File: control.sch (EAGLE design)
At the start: 68 parts, among them IC3 ATTINY85-20S, U1 L293DD013TR

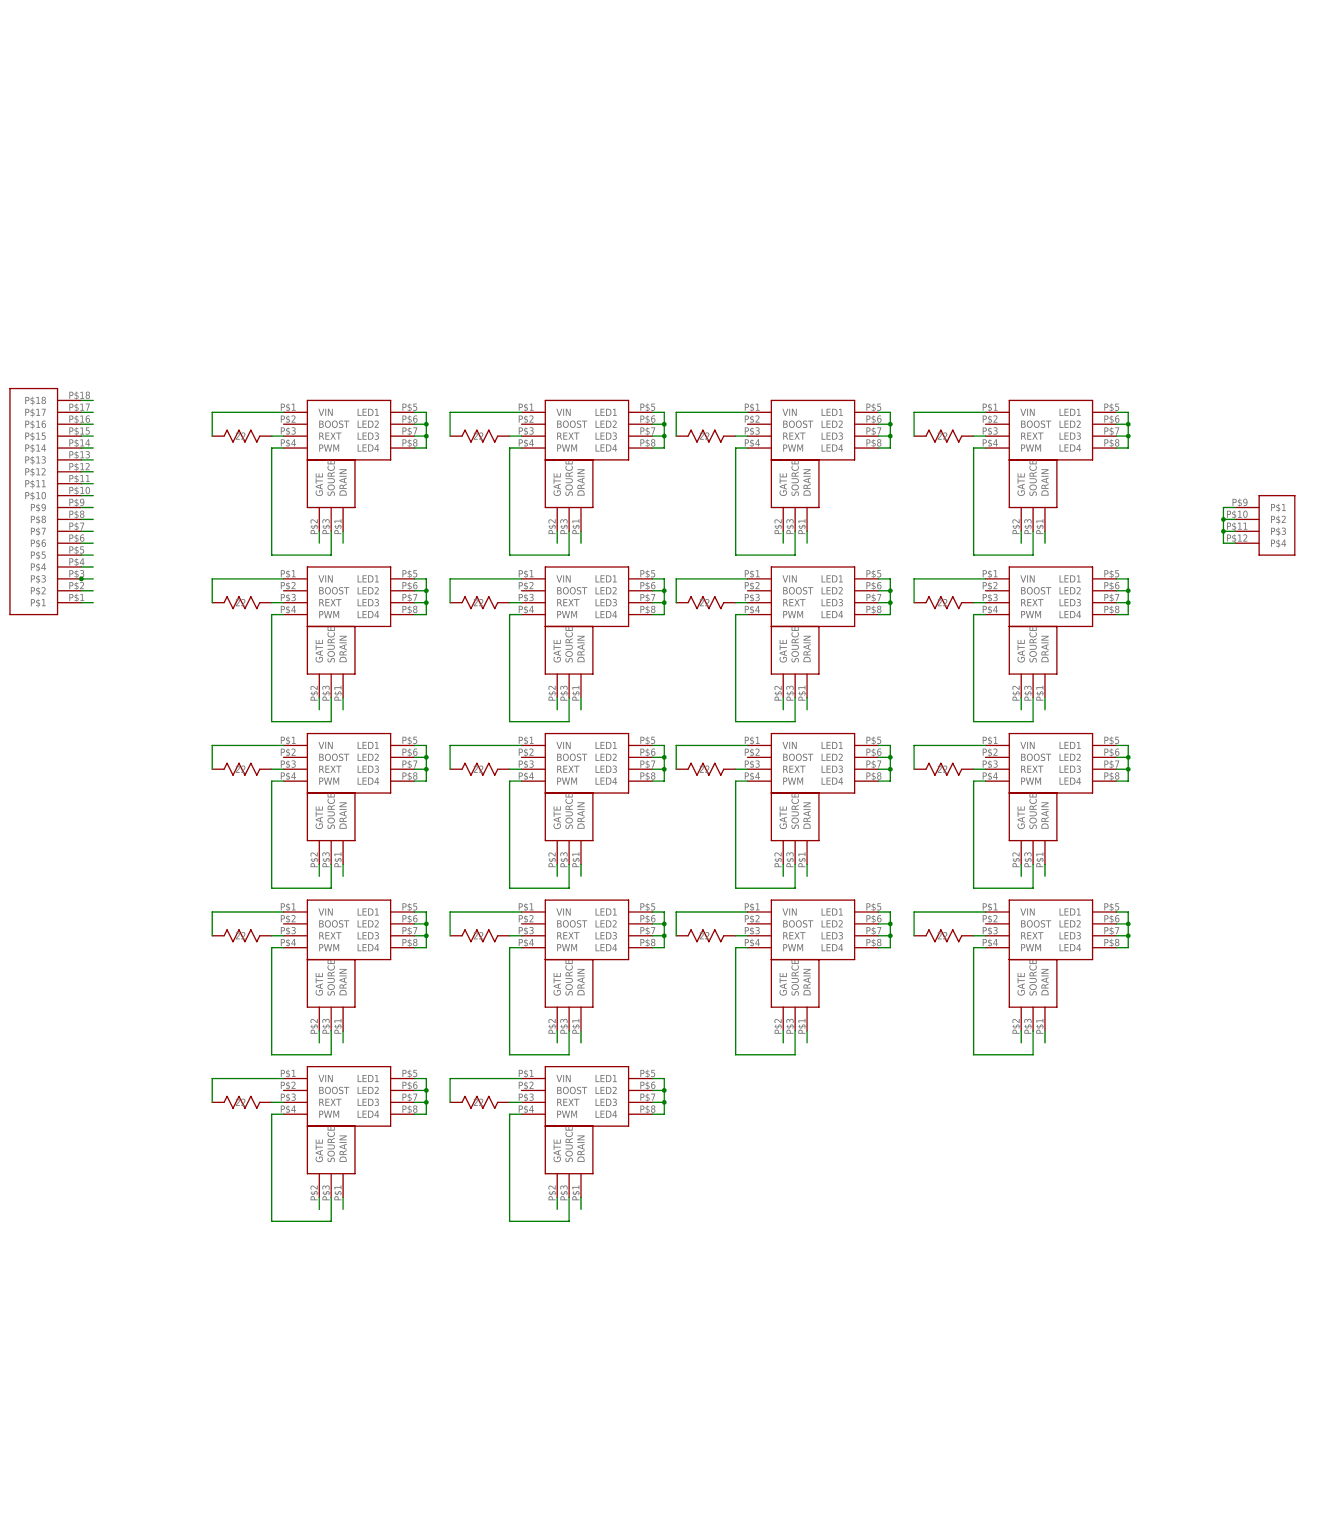
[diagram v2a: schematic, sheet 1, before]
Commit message: setts up warm cool LED support
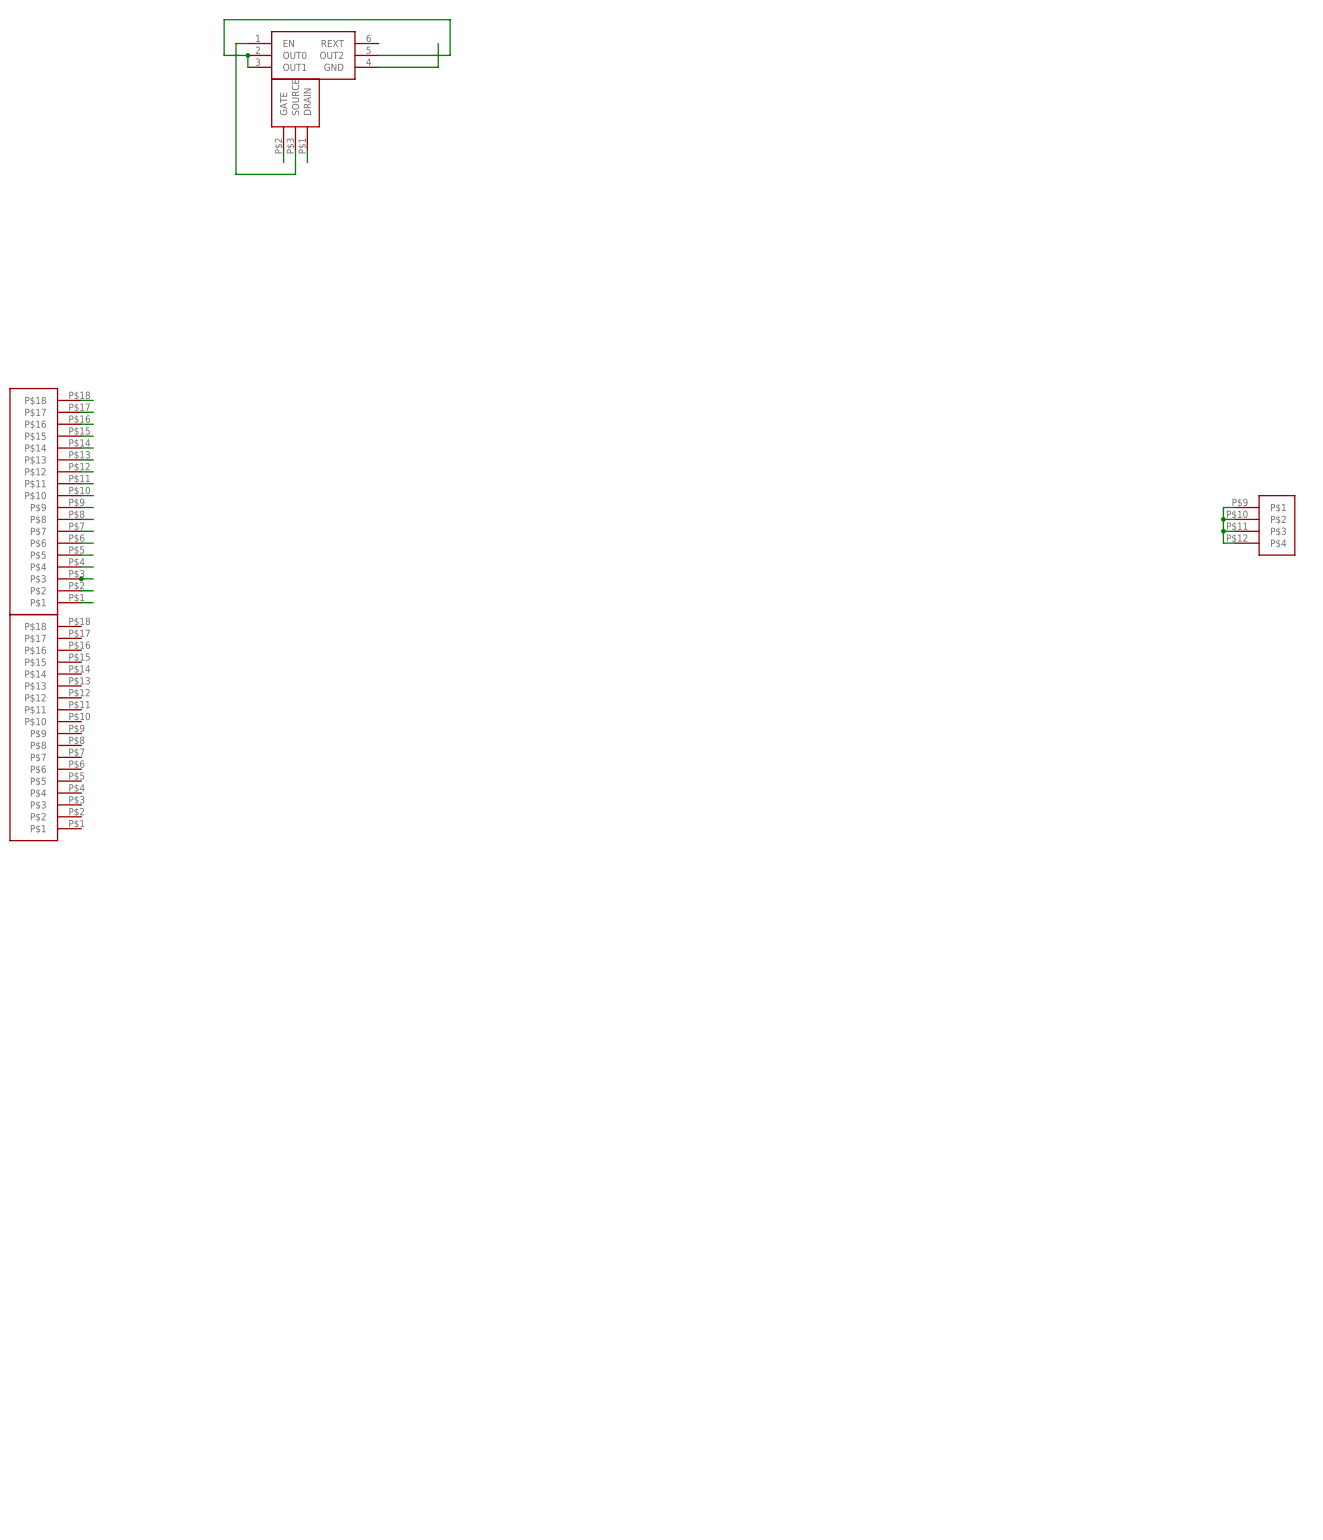
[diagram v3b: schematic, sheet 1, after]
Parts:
- removed R1, R10, R11, R12, R13, R14, R15, R16, R17, R19, R2, R3, R4, R5, R6, R7, R8, R9: RC0603FR-0710RL, Smile_Shade:RC0603FR-0710RL
- removed U$10, U$12, U$14, U$16, U$18, U$20, U$22, U$24, U$26, U$28, U$30, U$32, U$34, U$4, U$41, U$6, U$8: 2N7002P, Smile_Shade:2N7002P
- removed U$11, U$13, U$15, U$17, U$19, U$21, U$23, U$25, U$27, U$29, U$3, U$31, U$33, U$35, U$40, U$5, U$7, U$9: NUD4011DR2G, Smile_Shade:NUD4011DR2G
- added U$2: BCR420UW6-7, Smile_Shade:BCR420UW6-7
- added U$80: SFV18R-3STBE1HLF, Smile_Shade:SFV18R-3STBE1HLF
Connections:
- removed net 48: R16.22, U$35.VIN
- removed net N$1: U$3.PWM, U$4.SOURCE
- removed net N$10: R4.11, U$11.REXT
- removed net N$11: U$12.SOURCE, U$13.PWM
- removed net N$12: R5.11, U$13.REXT
- removed net N$13: U$10.SOURCE, U$15.PWM
- removed net N$14: R6.11, U$15.REXT
- removed net N$15: U$17.PWM, U$38.SOURCE
- removed net N$16: R8.11, U$17.REXT
- removed net N$17: U$18.SOURCE, U$25.PWM
- removed net N$18: R7.11, U$25.REXT
- removed net N$19: U$20.SOURCE, U$23.PWM
- removed net N$20: R9.11, U$23.REXT
- removed net N$21: U$21.PWM, U$22.SOURCE
- removed net N$22: R10.11, U$21.REXT
- removed net N$23: U$19.PWM, U$24.SOURCE
- removed net N$24: R11.11, U$19.REXT
- removed net N$25: U$27.PWM, U$32.SOURCE
- removed net N$26: R15.11, U$27.REXT
- removed net N$27: U$29.PWM, U$30.SOURCE
- removed net N$28: R14.11, U$29.REXT
- removed net N$29: U$28.SOURCE, U$31.PWM
- removed net N$3: U$5.PWM, U$6.SOURCE
- removed net N$30: R13.11, U$31.REXT
- removed net N$31: U$26.SOURCE, U$33.PWM
- removed net N$32: R12.11, U$33.REXT
- removed net N$35: U$34.SOURCE, U$35.PWM
- removed net N$36: R16.11, U$35.REXT
- removed net N$37: U$40.PWM, U$41.SOURCE
- removed net N$38: R17.11, U$40.REXT
- removed net N$4: R1.11, U$5.REXT
- removed net N$5: U$7.PWM, U$8.SOURCE
- removed net N$6: R2.11, U$7.REXT
- removed net N$7: U$16.SOURCE, U$9.PWM
- removed net N$8: R3.11, U$9.REXT
- removed net N$9: U$11.PWM, U$14.SOURCE
- removed net ZN16: U$41.GATE
- net 48V: no longer R1.22, R10.22, R11.22, R12.22, R13.22, R14.22, R15.22, R17.22, R19.22, R2.22, R3.22, R4.22, R5.22, R6.22, R7.22, R8.22, R9.22, U$11.VIN, U$13.VIN, U$15.VIN, U$17.VIN, U$19.VIN, U$21.VIN, U$23.VIN, U$25.VIN, U$27.VIN, U$29.VIN, U$3.VIN, U$31.VIN, U$33.VIN, U$40.VIN, U$5.VIN, U$7.VIN, U$9.VIN
- net GND: now also U$2.GND; no longer U$10.DRAIN, U$12.DRAIN, U$14.DRAIN, U$16.DRAIN, U$18.DRAIN, U$20.DRAIN, U$22.DRAIN, U$24.DRAIN, U$26.DRAIN, U$28.DRAIN, U$30.DRAIN, U$32.DRAIN, U$34.DRAIN, U$4.DRAIN, U$41.DRAIN, U$6.DRAIN, U$8.DRAIN
- net LEDSTR_1: now also U$2.OUT0, U$2.OUT1, U$2.OUT2; no longer U$17.LED1, U$17.LED2, U$17.LED3, U$17.LED4
- net LEDSTR_10: no longer U$23.LED1, U$23.LED2, U$23.LED3, U$23.LED4
- net LEDSTR_11: no longer U$21.LED1, U$21.LED2, U$21.LED3, U$21.LED4
- net LEDSTR_12: no longer U$19.LED1, U$19.LED2, U$19.LED3, U$19.LED4
- net LEDSTR_13: no longer U$27.LED1, U$27.LED2, U$27.LED3, U$27.LED4
- net LEDSTR_14: no longer U$29.LED1, U$29.LED2, U$29.LED3, U$29.LED4
- net LEDSTR_15: no longer U$31.LED1, U$31.LED2, U$31.LED3, U$31.LED4
- net LEDSTR_16: no longer U$33.LED1, U$33.LED2, U$33.LED3, U$33.LED4
- net LEDSTR_17: no longer U$35.LED1, U$35.LED2, U$35.LED3, U$35.LED4
- net LEDSTR_18: no longer U$40.LED1, U$40.LED2, U$40.LED3, U$40.LED4
- net LEDSTR_2: no longer U$3.LED1, U$3.LED2, U$3.LED3, U$3.LED4
- net LEDSTR_3: no longer U$5.LED1, U$5.LED2, U$5.LED3, U$5.LED4
- net LEDSTR_4: no longer U$7.LED1, U$7.LED2, U$7.LED3, U$7.LED4
- net LEDSTR_5: no longer U$9.LED1, U$9.LED2, U$9.LED3, U$9.LED4
- net LEDSTR_6: no longer U$11.LED1, U$11.LED2, U$11.LED3, U$11.LED4
- net LEDSTR_7: no longer U$13.LED1, U$13.LED2, U$13.LED3, U$13.LED4
- net LEDSTR_8: no longer U$15.LED1, U$15.LED2, U$15.LED3, U$15.LED4
- net LEDSTR_9: no longer U$25.LED1, U$25.LED2, U$25.LED3, U$25.LED4
- net N$2: now also U$2.EN, U$38.SOURCE; no longer R19.11, U$3.REXT
- net ZN1: no longer U$4.GATE
- net ZN10: no longer U$30.GATE
- net ZN11: no longer U$32.GATE
- net ZN12: no longer U$24.GATE
- net ZN13: no longer U$18.GATE
- net ZN14: no longer U$20.GATE
- net ZN15: no longer U$22.GATE
- net ZN2: no longer U$6.GATE
- net ZN3: no longer U$8.GATE
- net ZN4: no longer U$12.GATE
- net ZN5: no longer U$14.GATE
- net ZN6: no longer U$16.GATE
- net ZN7: no longer U$10.GATE
- net ZN8: no longer U$26.GATE, U$34.GATE
- net ZN9: no longer U$28.GATE

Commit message: Finalised-ish warm to cool dimming schematic
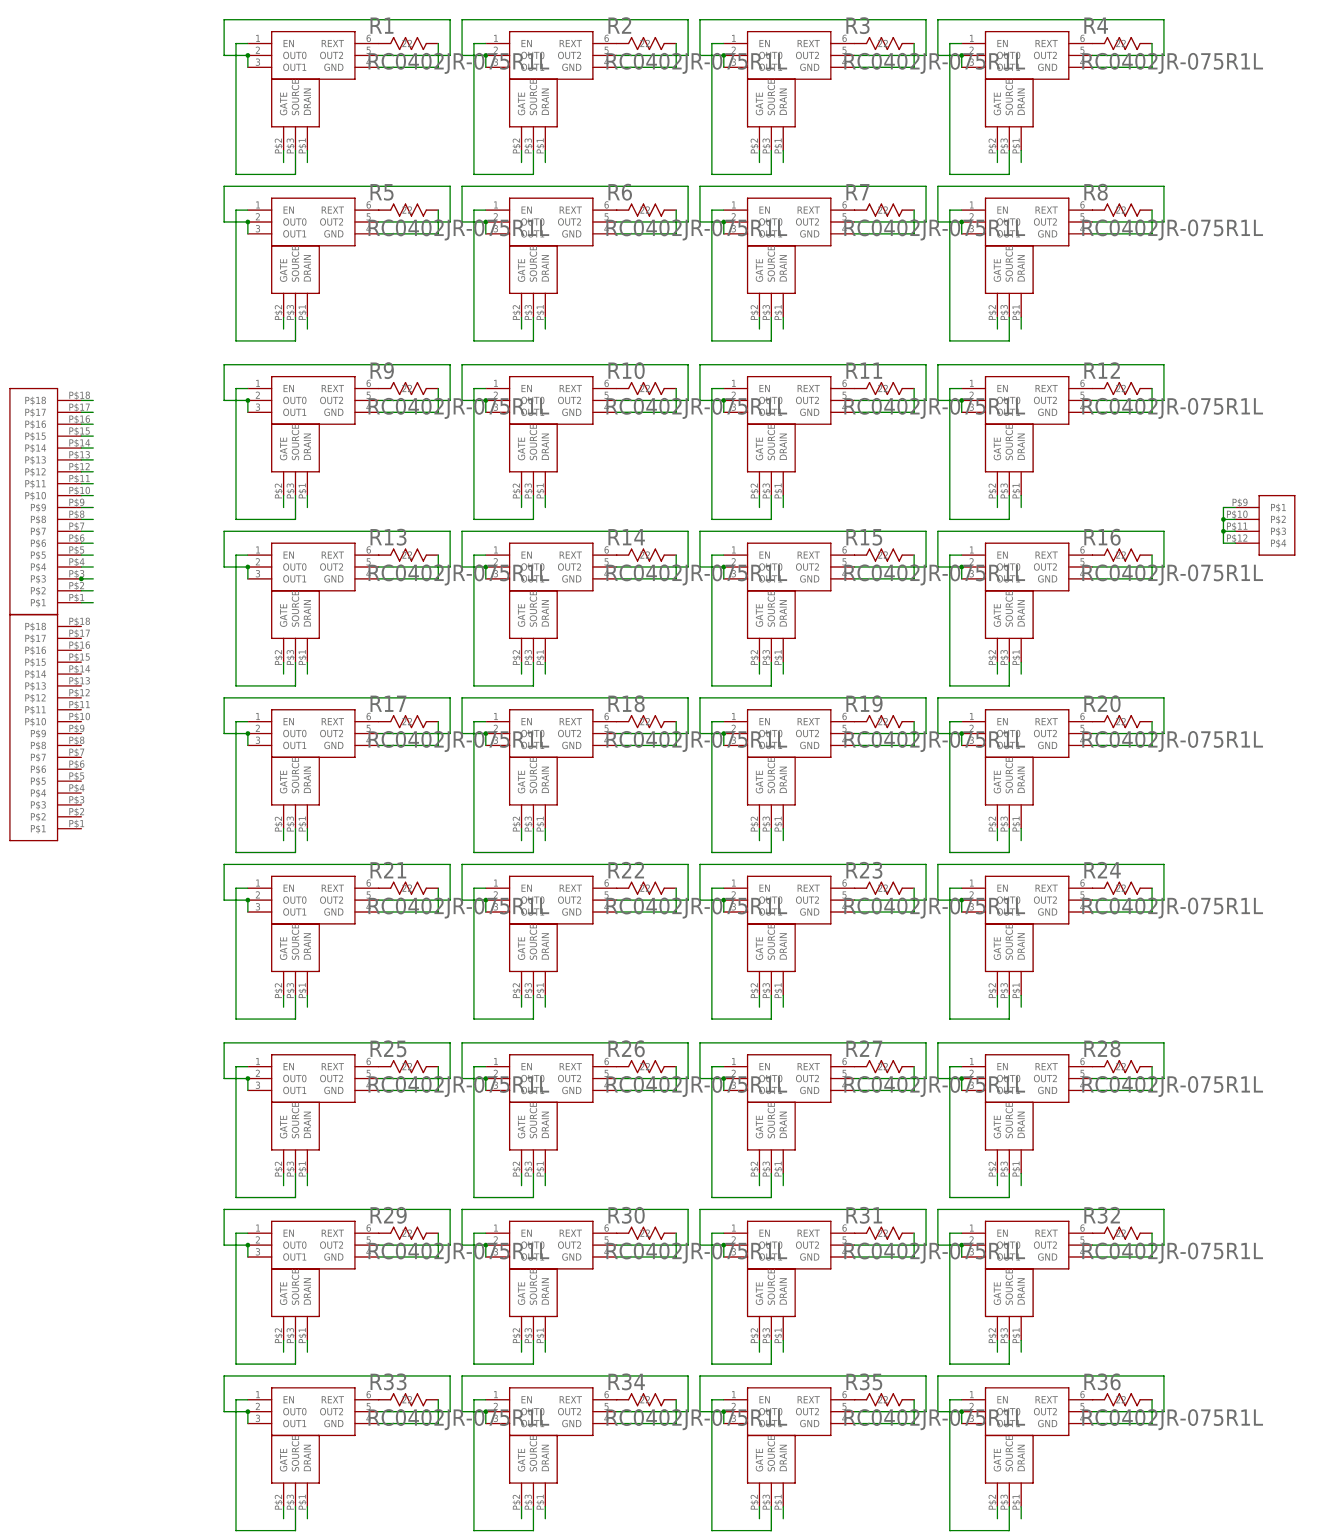
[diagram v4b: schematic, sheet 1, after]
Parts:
- added R1, R10, R11, R12, R13, R14, R15, R16, R17, R18, R19, R2, R20, R21, R22, R23, R24, R25, R26, R27, R28, R29, R3, R30, R31, R32, R33, R34, R35, R36, R4, R5, R6, R7, R8, R9: RC0402JR-075R1L, Smile_Shade:RC0402JR-075R1L
- added U$10, U$12, U$14, U$16, U$18, U$20, U$22, U$24, U$26, U$28, U$30, U$32, U$34, U$4, U$40, U$45, U$47, U$49, U$51, U$53, U$55, U$57, U$59, U$6, U$61, U$63, U$65, U$67, U$69, U$71, U$73, U$75, U$77, U$79, U$8: BCR420UW6-7, Smile_Shade:BCR420UW6-7
- added U$11, U$13, U$15, U$17, U$19, U$21, U$23, U$25, U$27, U$29, U$3, U$31, U$33, U$35, U$41, U$46, U$48, U$5, U$50, U$52, U$54, U$56, U$58, U$60, U$62, U$64, U$66, U$68, U$7, U$70, U$72, U$74, U$76, U$78, U$9: 2N7002P, Smile_Shade:2N7002P
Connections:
- new net GND1: R2.11, U$3.DRAIN, U$4.GND
- new net GND10: R11.11, U$21.DRAIN, U$22.GND
- new net GND11: R12.11, U$23.DRAIN, U$24.GND
- new net GND12: R13.11, U$25.DRAIN, U$26.GND
- new net GND13: R14.11, U$27.DRAIN, U$28.GND
- new net GND14: R15.11, U$29.DRAIN, U$30.GND
- new net GND15: R16.11, U$31.DRAIN, U$32.GND
- new net GND16: R17.11, U$33.DRAIN, U$34.GND
- new net GND17: R18.11, U$35.DRAIN, U$40.GND
- new net GND18: R19.11, U$41.DRAIN, U$45.GND
- new net GND19: R20.11, U$46.DRAIN, U$47.GND
- new net GND2: R3.11, U$5.DRAIN, U$6.GND
- new net GND20: R21.11, U$48.DRAIN, U$49.GND
- new net GND21: R22.11, U$50.DRAIN, U$51.GND
- new net GND22: R23.11, U$52.DRAIN, U$53.GND
- new net GND23: R24.11, U$54.DRAIN, U$55.GND
- new net GND24: R25.11, U$56.DRAIN, U$57.GND
- new net GND25: R26.11, U$58.DRAIN, U$59.GND
- new net GND26: R27.11, U$60.DRAIN, U$61.GND
- new net GND27: R28.11, U$62.DRAIN, U$63.GND
- new net GND28: R29.11, U$64.DRAIN, U$65.GND
- new net GND29: R30.11, U$66.DRAIN, U$67.GND
- new net GND3: R4.11, U$7.DRAIN, U$8.GND
- new net GND30: R31.11, U$68.DRAIN, U$69.GND
- new net GND31: R32.11, U$70.DRAIN, U$71.GND
- new net GND32: R33.11, U$72.DRAIN, U$73.GND
- new net GND33: R34.11, U$74.DRAIN, U$75.GND
- new net GND34: R35.11, U$76.DRAIN, U$77.GND
- new net GND35: R36.11, U$78.DRAIN, U$79.GND
- new net GND4: R5.11, U$10.GND, U$9.DRAIN
- new net GND5: R6.11, U$11.DRAIN, U$12.GND
- new net GND6: R7.11, U$13.DRAIN, U$14.GND
- new net GND7: R8.11, U$15.DRAIN, U$16.GND
- new net GND8: R9.11, U$17.DRAIN, U$18.GND
- new net GND9: R10.11, U$19.DRAIN, U$20.GND
- new net LEDSTR_19: U$10.OUT0, U$10.OUT1, U$10.OUT2
- new net LEDSTR_20: U$12.OUT0, U$12.OUT1, U$12.OUT2
- new net LEDSTR_21: U$14.OUT0, U$14.OUT1, U$14.OUT2
- new net LEDSTR_22: U$16.OUT0, U$16.OUT1, U$16.OUT2
- new net LEDSTR_23: U$18.OUT0, U$18.OUT1, U$18.OUT2
- new net LEDSTR_24: U$20.OUT0, U$20.OUT1, U$20.OUT2
- new net LEDSTR_25: U$22.OUT0, U$22.OUT1, U$22.OUT2
- new net LEDSTR_26: U$24.OUT0, U$24.OUT1, U$24.OUT2
- new net LEDSTR_27: U$26.OUT0, U$26.OUT1, U$26.OUT2
- new net LEDSTR_28: U$28.OUT0, U$28.OUT1, U$28.OUT2
- new net LEDSTR_29: U$30.OUT0, U$30.OUT1, U$30.OUT2
- new net LEDSTR_30: U$32.OUT0, U$32.OUT1, U$32.OUT2
- new net LEDSTR_31: U$34.OUT0, U$34.OUT1, U$34.OUT2
- new net LEDSTR_32: U$40.OUT0, U$40.OUT1, U$40.OUT2
- new net LEDSTR_33: U$45.OUT0, U$45.OUT1, U$45.OUT2
- new net LEDSTR_34: U$47.OUT0, U$47.OUT1, U$47.OUT2
- new net LEDSTR_35: U$49.OUT0, U$49.OUT1, U$49.OUT2
- new net LEDSTR_36: U$51.OUT0, U$51.OUT1, U$51.OUT2
- new net LEDSTR_37: U$53.OUT0, U$53.OUT1, U$53.OUT2
- new net LEDSTR_38: U$55.OUT0, U$55.OUT1, U$55.OUT2
- new net LEDSTR_39: U$57.OUT0, U$57.OUT1, U$57.OUT2
- new net LEDSTR_40: U$59.OUT0, U$59.OUT1, U$59.OUT2
- new net LEDSTR_41: U$61.OUT0, U$61.OUT1, U$61.OUT2
- new net LEDSTR_42: U$63.OUT0, U$63.OUT1, U$63.OUT2
- new net LEDSTR_43: U$65.OUT0, U$65.OUT1, U$65.OUT2
- new net LEDSTR_44: U$67.OUT0, U$67.OUT1, U$67.OUT2
- new net LEDSTR_45: U$69.OUT0, U$69.OUT1, U$69.OUT2
- new net LEDSTR_46: U$71.OUT0, U$71.OUT1, U$71.OUT2
- new net LEDSTR_47: U$73.OUT0, U$73.OUT1, U$73.OUT2
- new net LEDSTR_48: U$75.OUT0, U$75.OUT1, U$75.OUT2
- new net LEDSTR_49: U$77.OUT0, U$77.OUT1, U$77.OUT2
- new net LEDSTR_50: U$79.OUT0, U$79.OUT1, U$79.OUT2
- new net N$1: R1.22, U$2.REXT
- new net N$10: R5.22, U$10.REXT
- new net N$11: U$11.SOURCE, U$12.EN
- new net N$12: R6.22, U$12.REXT
- new net N$13: U$13.SOURCE, U$14.EN
- new net N$14: R7.22, U$14.REXT
- new net N$15: U$15.SOURCE, U$16.EN
- new net N$16: R8.22, U$16.REXT
- new net N$17: U$17.SOURCE, U$18.EN
- new net N$18: R9.22, U$18.REXT
- new net N$19: U$19.SOURCE, U$20.EN
- new net N$20: R10.22, U$20.REXT
- new net N$21: U$21.SOURCE, U$22.EN
- new net N$22: R11.22, U$22.REXT
- new net N$23: U$23.SOURCE, U$24.EN
- new net N$24: R12.22, U$24.REXT
- new net N$25: U$25.SOURCE, U$26.EN
- new net N$26: R13.22, U$26.REXT
- new net N$27: U$27.SOURCE, U$28.EN
- new net N$28: R14.22, U$28.REXT
- new net N$29: U$29.SOURCE, U$30.EN
- new net N$3: U$3.SOURCE, U$4.EN
- new net N$30: R15.22, U$30.REXT
- new net N$31: U$31.SOURCE, U$32.EN
- new net N$32: R16.22, U$32.REXT
- new net N$35: U$33.SOURCE, U$34.EN
- new net N$36: R17.22, U$34.REXT
- new net N$37: U$35.SOURCE, U$40.EN
- new net N$38: R18.22, U$40.REXT
- new net N$4: R2.22, U$4.REXT
- new net N$42: U$41.SOURCE, U$45.EN
- new net N$43: R19.22, U$45.REXT
- new net N$44: U$46.SOURCE, U$47.EN
- new net N$45: R20.22, U$47.REXT
- new net N$46: U$48.SOURCE, U$49.EN
- new net N$47: R21.22, U$49.REXT
- new net N$48: U$50.SOURCE, U$51.EN
- new net N$49: R22.22, U$51.REXT
- new net N$5: U$5.SOURCE, U$6.EN
- new net N$50: U$52.SOURCE, U$53.EN
- new net N$51: R23.22, U$53.REXT
- new net N$52: U$54.SOURCE, U$55.EN
- new net N$53: R24.22, U$55.REXT
- new net N$54: U$56.SOURCE, U$57.EN
- new net N$55: R25.22, U$57.REXT
- new net N$56: U$58.SOURCE, U$59.EN
- new net N$57: R26.22, U$59.REXT
- new net N$58: U$60.SOURCE, U$61.EN
- new net N$59: R27.22, U$61.REXT
- new net N$6: R3.22, U$6.REXT
- new net N$60: U$62.SOURCE, U$63.EN
- new net N$61: R28.22, U$63.REXT
- new net N$62: U$64.SOURCE, U$65.EN
- new net N$63: R29.22, U$65.REXT
- new net N$64: U$66.SOURCE, U$67.EN
- new net N$65: R30.22, U$67.REXT
- new net N$66: U$68.SOURCE, U$69.EN
- new net N$67: R31.22, U$69.REXT
- new net N$68: U$70.SOURCE, U$71.EN
- new net N$69: R32.22, U$71.REXT
- new net N$7: U$7.SOURCE, U$8.EN
- new net N$70: U$72.SOURCE, U$73.EN
- new net N$71: R33.22, U$73.REXT
- new net N$72: U$74.SOURCE, U$75.EN
- new net N$73: R34.22, U$75.REXT
- new net N$74: U$76.SOURCE, U$77.EN
- new net N$75: R35.22, U$77.REXT
- new net N$76: U$78.SOURCE, U$79.EN
- new net N$77: R36.22, U$79.REXT
- new net N$8: R4.22, U$8.REXT
- new net N$9: U$10.EN, U$9.SOURCE
- new net ZN16: U$3.GATE
- new net ZN17: U$5.GATE
- new net ZN18: U$7.GATE
- new net ZN19: U$9.GATE
- new net ZN20: U$11.GATE
- new net ZN21: U$13.GATE
- new net ZN22: U$15.GATE
- new net ZN23: U$17.GATE
- new net ZN24: U$19.GATE
- new net ZN25: U$21.GATE
- new net ZN26: U$23.GATE
- new net ZN27: U$25.GATE
- new net ZN28: U$27.GATE
- new net ZN29: U$29.GATE
- new net ZN30: U$31.GATE
- new net ZN31: U$33.GATE
- new net ZN32: U$35.GATE
- new net ZN33: U$41.GATE
- new net ZN34: U$46.GATE
- new net ZN35: U$48.GATE
- new net ZN36: U$50.GATE
- new net ZN37: U$52.GATE
- new net ZN38: U$54.GATE
- new net ZN39: U$56.GATE
- new net ZN40: U$58.GATE
- new net ZN41: U$60.GATE
- new net ZN42: U$62.GATE
- new net ZN43: U$64.GATE
- new net ZN44: U$66.GATE
- new net ZN45: U$68.GATE
- new net ZN46: U$70.GATE
- new net ZN47: U$72.GATE
- new net ZN48: U$74.GATE
- new net ZN49: U$76.GATE
- new net ZN50: U$78.GATE
- net GND: now also R1.11
- net LEDSTR_2: now also U$4.OUT0, U$4.OUT1, U$4.OUT2
- net LEDSTR_3: now also U$6.OUT0, U$6.OUT1, U$6.OUT2
- net LEDSTR_4: now also U$8.OUT0, U$8.OUT1, U$8.OUT2
